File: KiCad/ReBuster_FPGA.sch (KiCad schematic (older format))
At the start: 25 parts, among them U1 10M02SCU169, U2 LM1117-3.3

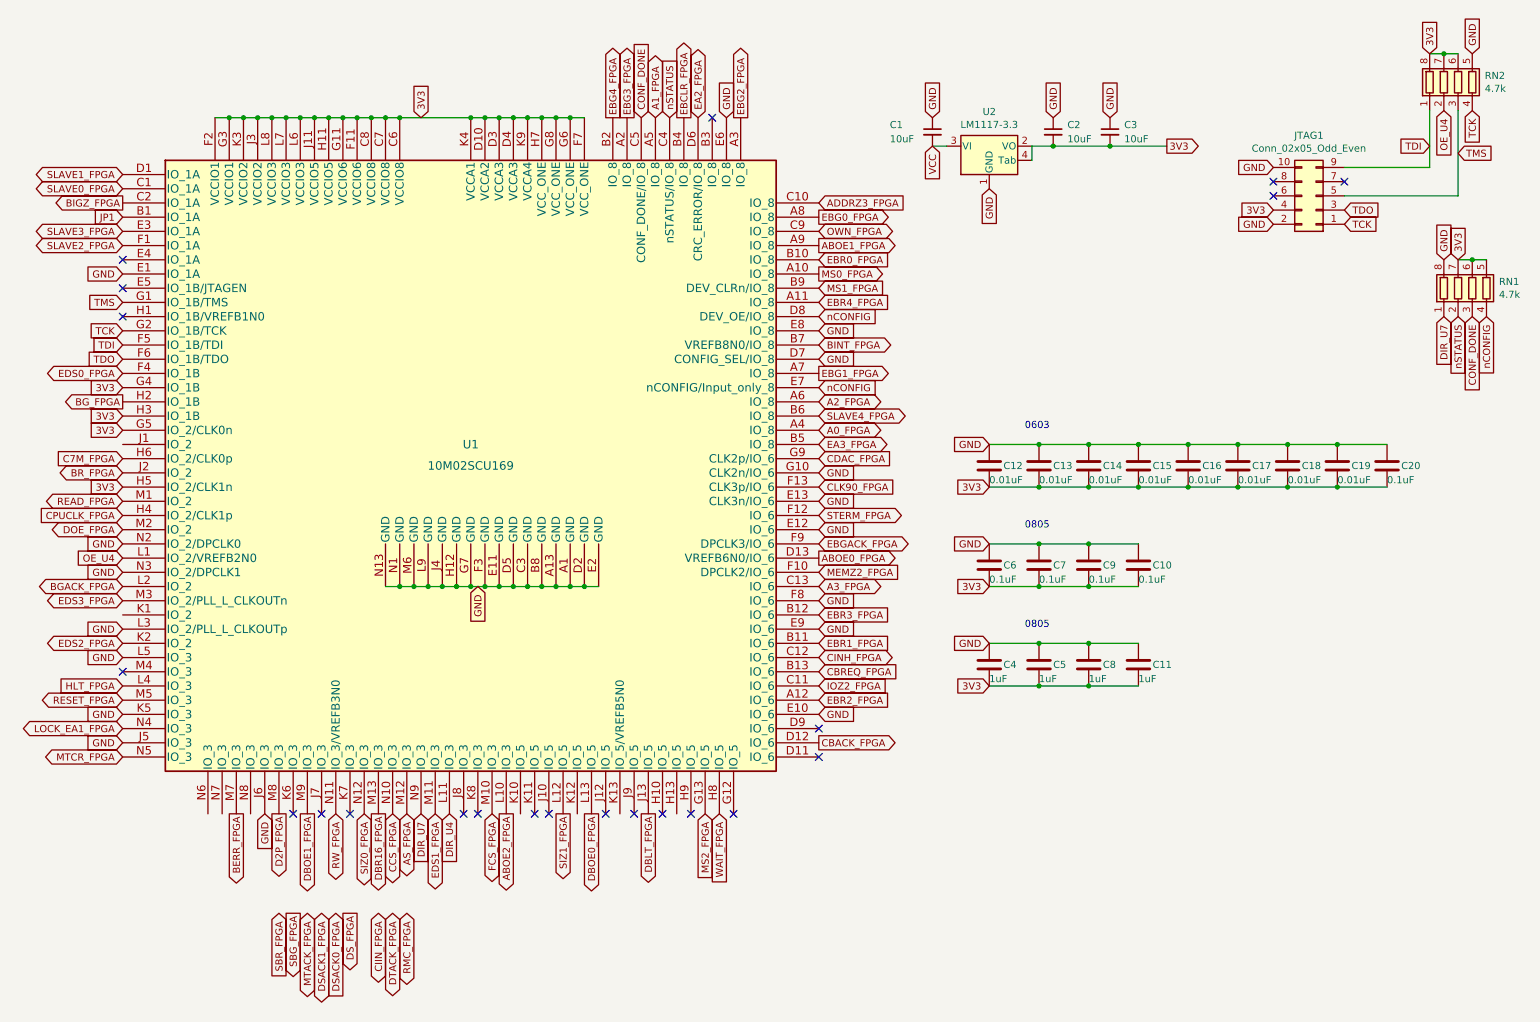
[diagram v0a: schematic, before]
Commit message: Route EA2,EA3 to U4 (SN74LVC16T245DGVR) change D6 -> N6, B5 -> N7 in FPGA
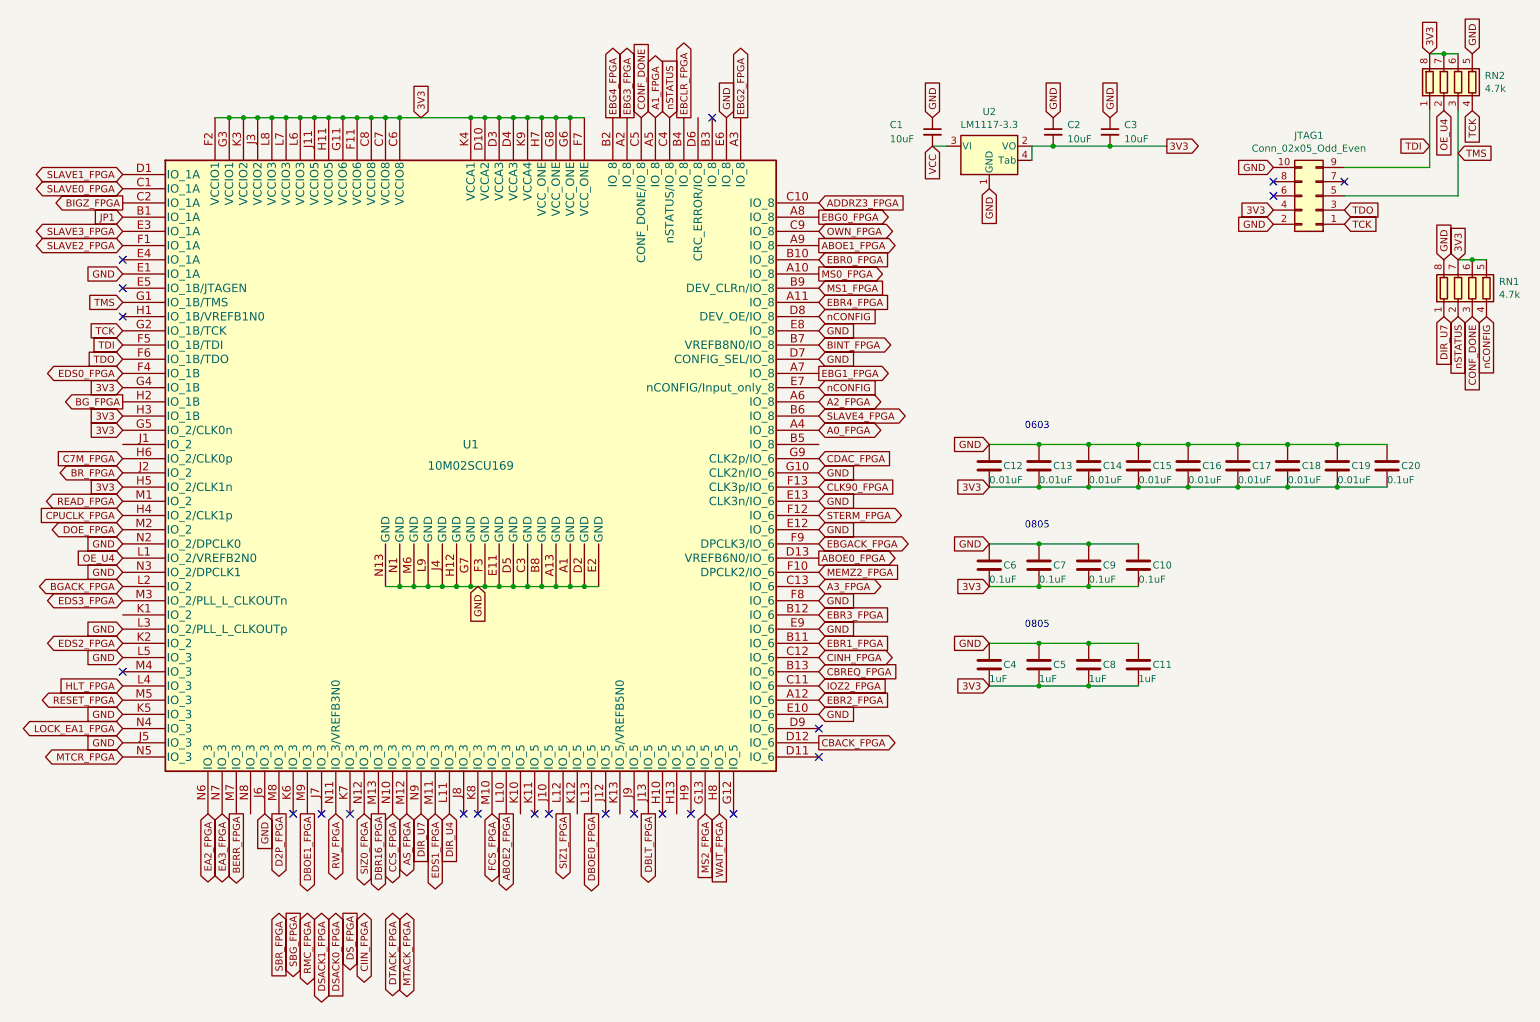
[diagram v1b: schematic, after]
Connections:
- net EA2_FPGA: now also U1.N6 (IO_3); no longer U1.D6 (CRC_ERROR/IO_8)
- net EA3_FPGA: now also U1.N7 (IO_3); no longer U1.B5 (IO_8)
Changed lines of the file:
@@
 Text GLabel 3050 6900 3    50   BiDi ~ 0
 DTACK_FPGA
-Text GLabel 2450 6900 3    50   BiDi ~ 0
+Text GLabel 3150 6900 3    50   BiDi ~ 0
 MTACK_FPGA
-Text GLabel 2950 6900 3    50   BiDi ~ 0
+Text GLabel 2850 6900 3    50   BiDi ~ 0
 CIIN_FPGA
 Text GLabel 2250 6900 3    50   Input ~ 0
 SBR_FPGA
-Text GLabel 3150 6900 3    50   BiDi ~ 0
+Text GLabel 2450 6900 3    50   BiDi ~ 0
 RMC_FPGA
 Text GLabel 3050 6200 3    50   BiDi ~ 0
@@
 Text GLabel 1150 3100 0    50   BiDi ~ 0
 EDS0_FPGA
-Text GLabel 6050 3600 2    50   BiDi ~ 0
+Text GLabel 1850 6200 3    50   BiDi ~ 0
 EA3_FPGA
-Text GLabel 5200 1300 1    50   BiDi ~ 0
+Text GLabel 1750 6200 3    50   BiDi ~ 0
 EA2_FPGA
 Text GLabel 6050 4300 2    50   BiDi ~ 0

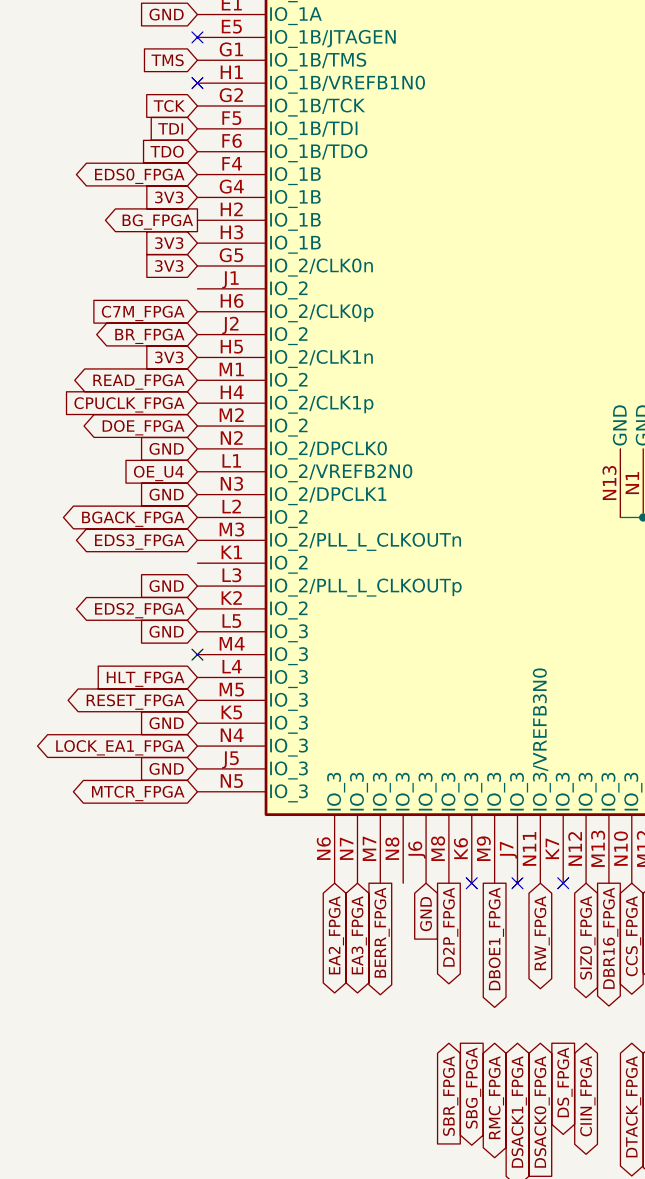
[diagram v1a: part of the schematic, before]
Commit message: Route EDS0 to U4 (SN74LVC16T245DGVR) change F4 -> N8 in FPGA
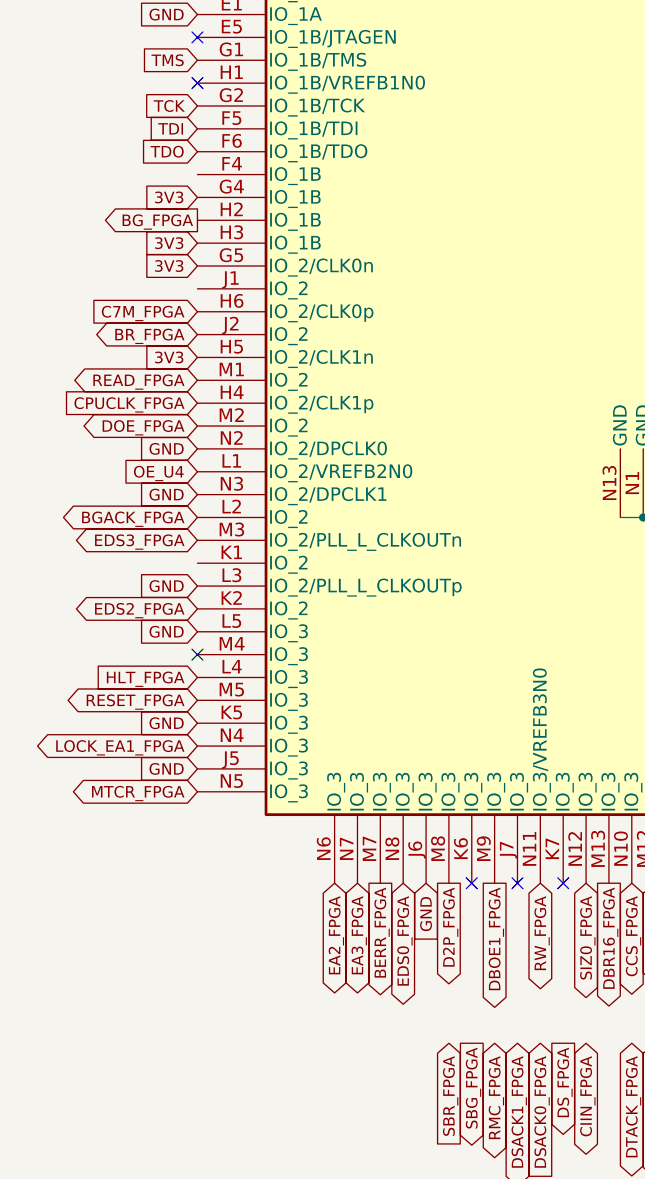
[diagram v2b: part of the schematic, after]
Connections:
- net EDS0_FPGA: now also U1.N8 (IO_3); no longer U1.F4 (IO_1B)
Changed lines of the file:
@@
 Text GLabel 5100 1300 1    50   Output ~ 0
 EBCLR_FPGA
-Text GLabel 1150 3100 0    50   BiDi ~ 0
+Text GLabel 2050 6200 3    50   BiDi ~ 0
 EDS0_FPGA
 Text GLabel 1850 6200 3    50   BiDi ~ 0

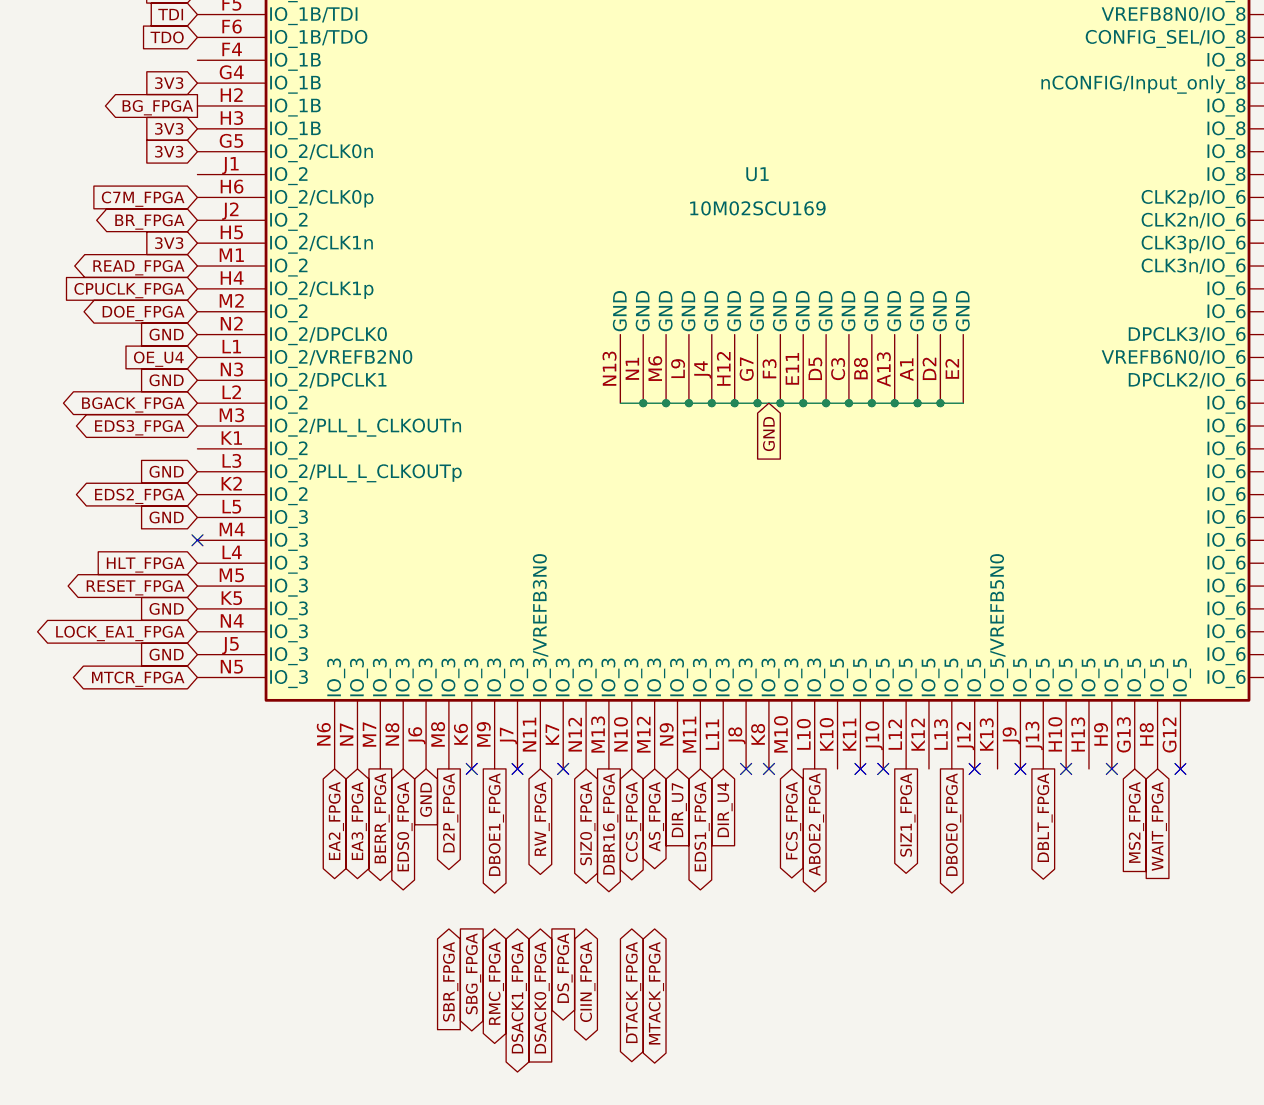
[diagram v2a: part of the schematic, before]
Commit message: Route RMC, SBR, SBG, CIIN to U6 (SN74CBTD16210) and assign pins K10, K11, K12, H13 in FPGA respectively
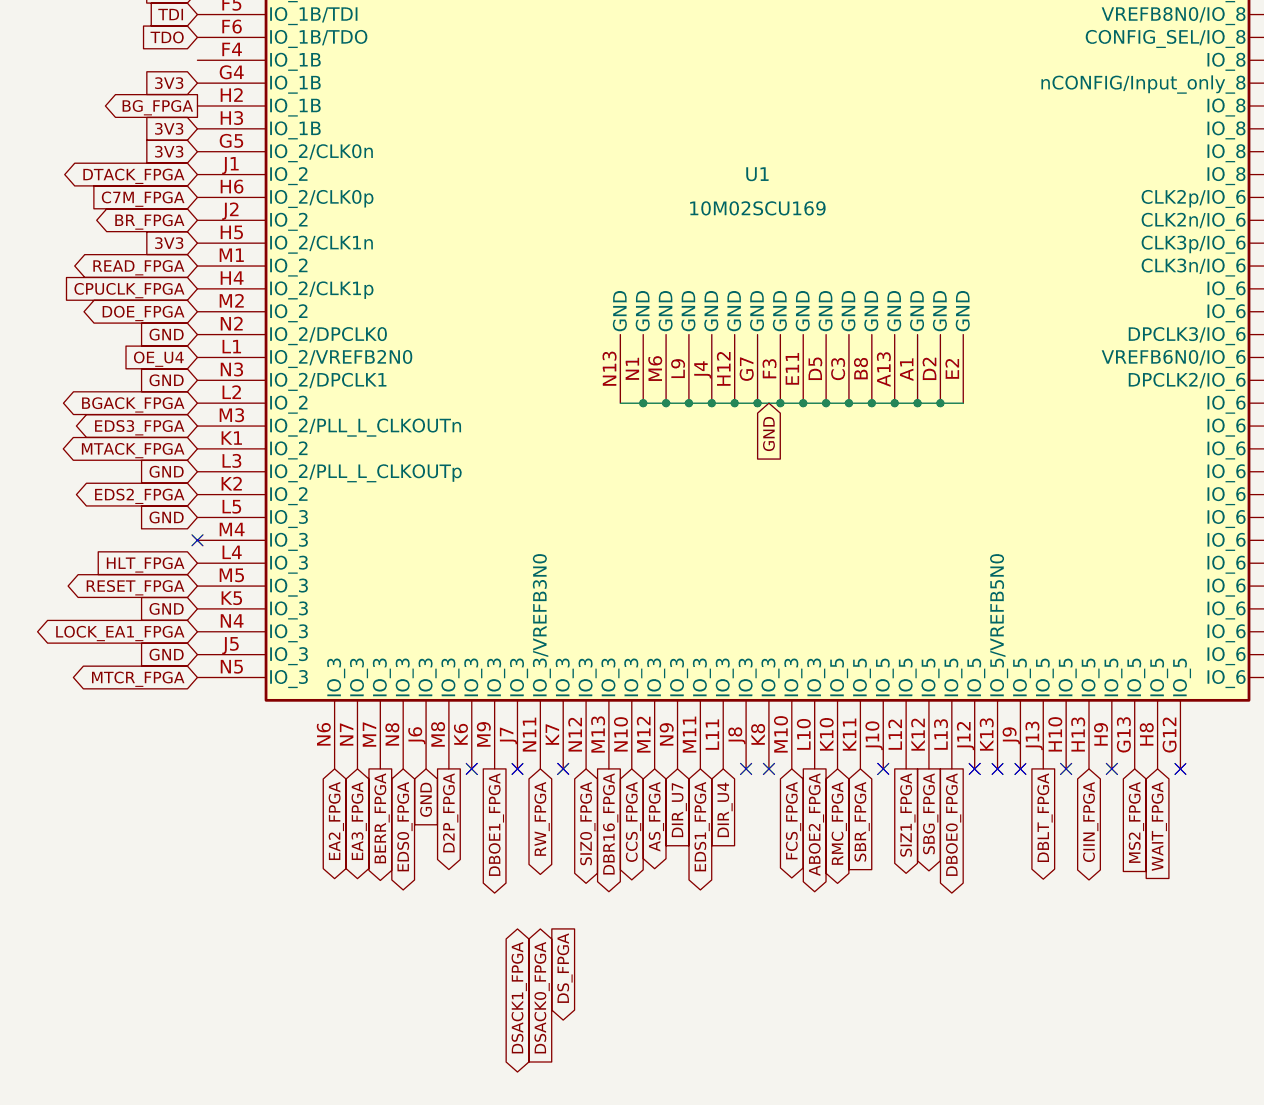
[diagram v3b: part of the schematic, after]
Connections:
- net CIIN_FPGA: now also U1.H13 (IO_5)
- net DTACK_FPGA: now also U1.J1 (IO_2)
- net MTACK_FPGA: now also U1.K1 (IO_2)
- net RMC_FPGA: now also U1.K10 (IO_5)
- net SBG_FPGA: now also U1.K12 (IO_5)
- net SBR_FPGA: now also U1.K11 (IO_5)
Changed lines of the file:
@@
 Text GLabel 1150 4200 0    50   BiDi ~ 0
 DOE_FPGA
-Text GLabel 3050 6900 3    50   BiDi ~ 0
+Text GLabel 1150 3600 0    50   BiDi ~ 0
 DTACK_FPGA
-Text GLabel 3150 6900 3    50   BiDi ~ 0
+Text GLabel 1150 4800 0    50   BiDi ~ 0
 MTACK_FPGA
-Text GLabel 2850 6900 3    50   BiDi ~ 0
+Text GLabel 5050 6200 3    50   BiDi ~ 0
 CIIN_FPGA
-Text GLabel 2250 6900 3    50   Input ~ 0
+Text GLabel 4050 6200 3    50   Input ~ 0
 SBR_FPGA
-Text GLabel 2450 6900 3    50   BiDi ~ 0
+Text GLabel 3950 6200 3    50   BiDi ~ 0
 RMC_FPGA
 Text GLabel 3050 6200 3    50   BiDi ~ 0
@@
 Text GLabel 4900 1300 1    50   BiDi ~ 0
 A1_FPGA
-Text GLabel 2350 6900 3    50   Output ~ 0
+Text GLabel 4350 6200 3    50   Output ~ 0
 SBG_FPGA
 Text GLabel 2650 6200 3    50   BiDi ~ 0
@@
 NoConn ~ 2750 6200
 NoConn ~ 3550 6200
-NoConn ~ 4050 6200
 NoConn ~ 4150 6200
 NoConn ~ 4550 6200
@@
 Text GLabel 1150 4400 0    50   Input ~ 0
 OE_U4
+NoConn ~ 4650 6200
 $EndSCHEMATC
